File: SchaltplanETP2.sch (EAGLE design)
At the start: 59 parts, among them IC1 LM2674, IC2 ZXLD1350, IC3 ZXLD1350, IC4 ZXLD1350, IC5 ZXLD1350, M1 RN42_BLUETOOTH, T1 BUK98150-55A

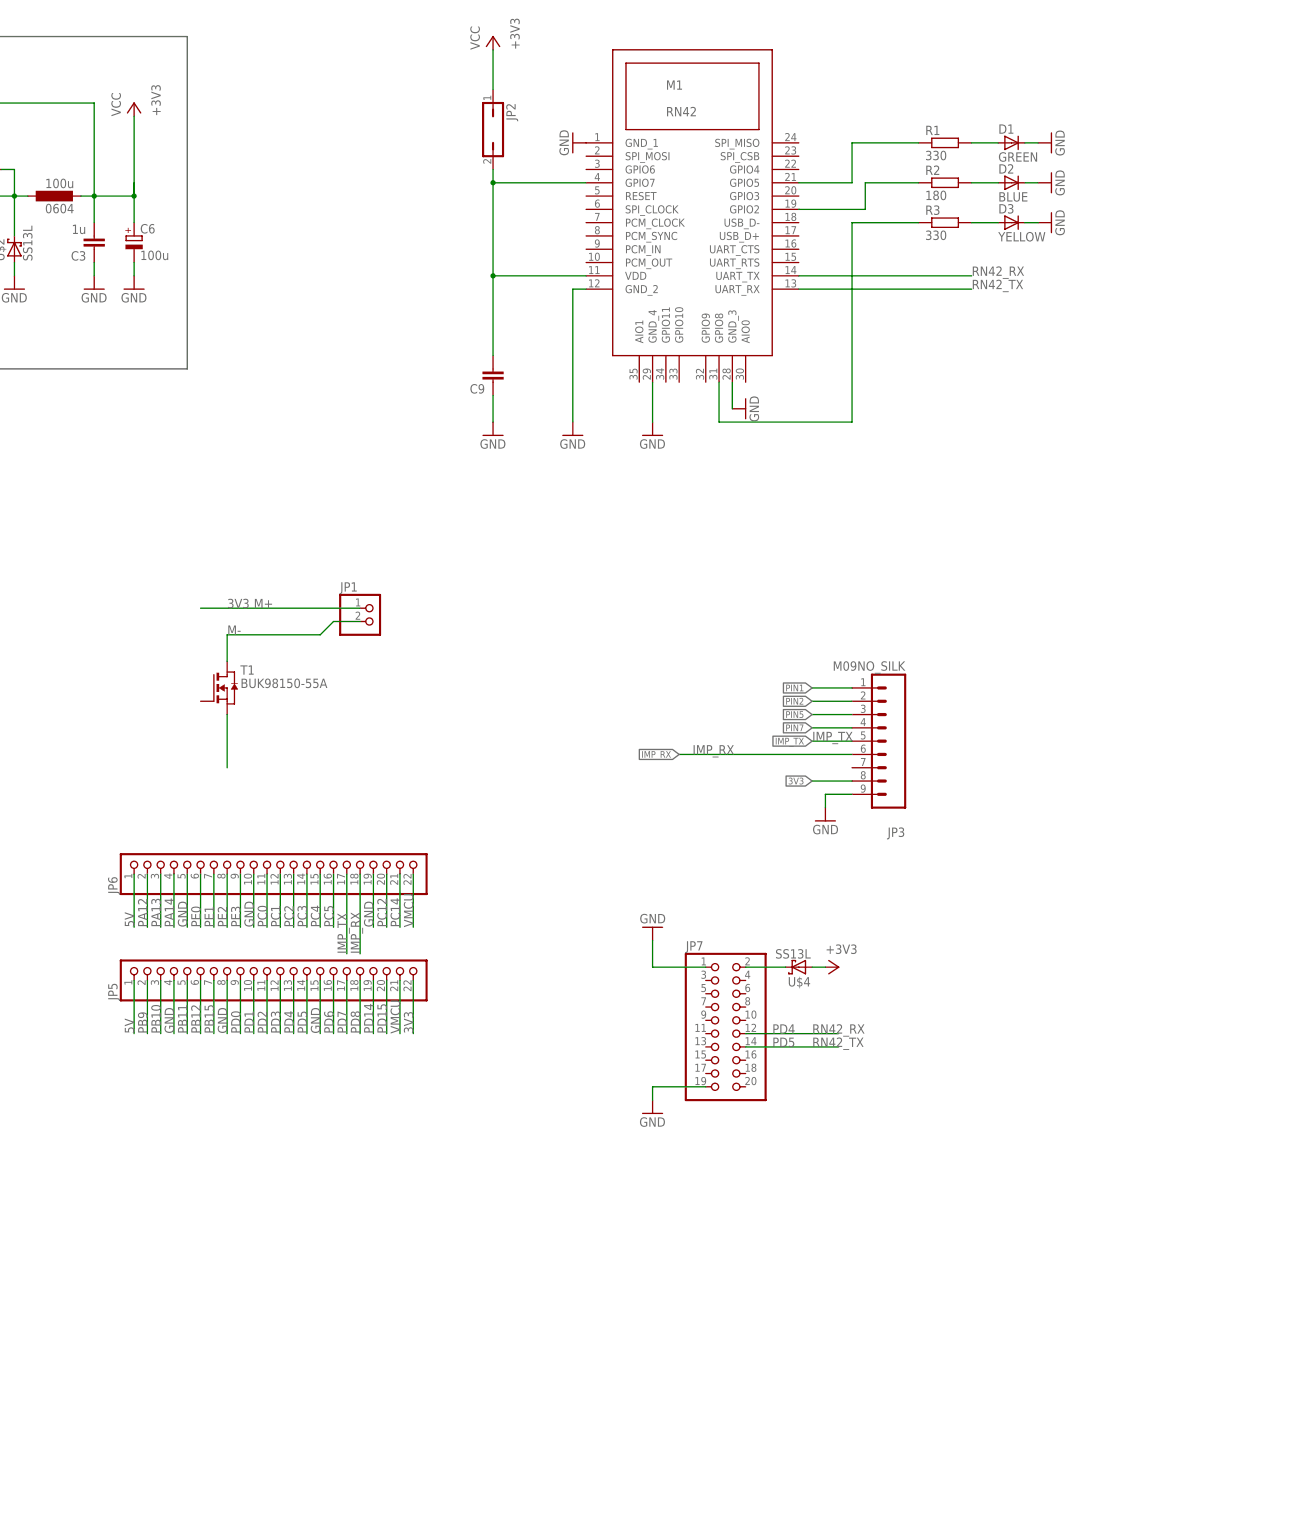
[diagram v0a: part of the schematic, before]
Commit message: Changed LED of pin 21 from the RN42 module to fit the datasheet. Added Jumpber behind DC-Jack to allow direct soldering of cables. Added Terminal Blocks for LEDs.
Placed part onto grid.
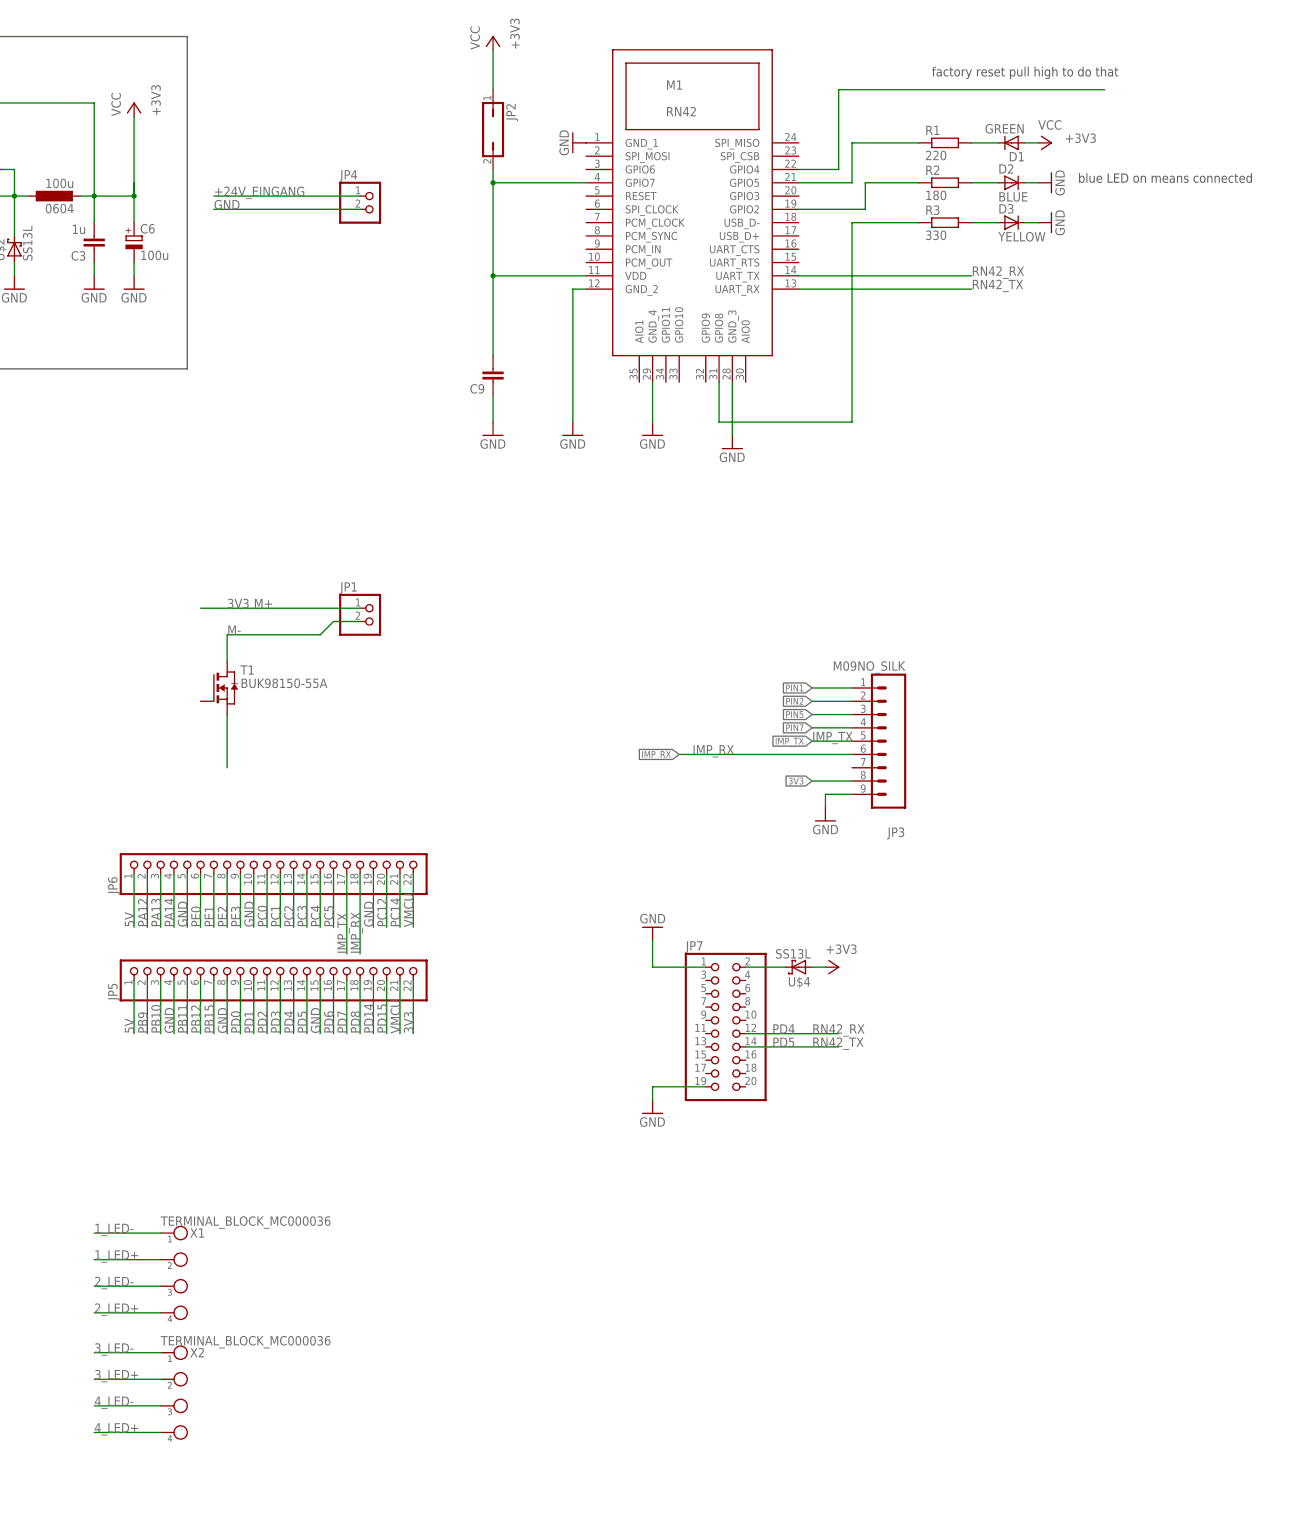
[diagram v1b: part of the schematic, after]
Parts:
- added JP4: (no value), pinhead:PINHD-1X2
- added X1, X2: TERMINAL_BLOCK_MC000036, Moodlight:TERMINAL_BLOCK_MC000036
- R1: value 330 -> 220
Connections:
- removed net N$1: U$1.A, U$3.1
- new net +24V_EINGANG: JP4.1, U$1.A, U$3.1
- new net 4_LED+: X2.4
- new net 4_LED-: X2.3
- new net N$21: M1.GPIO4
- net +3V3: now also D1.A
- net 1_LED+: now also X1.2
- net 1_LED-: now also X1.1
- net 2_LED+: now also X1.4
- net 2_LED-: now also X1.3
- net 3_LED+: now also X2.2
- net 3_LED-: now also X2.1
- net GND: now also JP4.2; no longer D1.C
- net N$7: now also D1.C; no longer D1.A
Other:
- note added: "blue LED on means connected"
- note added: "factory reset pull high to do that"
- moved on the sheet: D1
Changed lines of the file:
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@@
 <layer number="91" name="Nets" color="2" fill="1" visible="yes" active="yes"/>
 <layer number="92" name="Busses" color="1" fill="1" visible="yes" active="yes"/>
-<layer number="93" name="Pins" color="2" fill="1" visible="yes" active="yes"/>
+<layer number="93" name="Pins" color="2" fill="1" visible="no" active="yes"/>
 <layer number="94" name="Symbols" color="4" fill="1" visible="yes" active="yes"/>
 <layer number="95" name="Names" color="7" fill="1" visible="yes" active="yes"/>
@@
 <part name="GND16" library="supply1" deviceset="GND" device=""/>
 <part name="GND17" library="supply1" deviceset="GND" device=""/>
-<part name="GND18" library="supply1" deviceset="GND" device=""/>
 <part name="JP2" library="jumper" deviceset="JP1Q" device=""/>
 <part name="P+2" library="supply1" deviceset="VCC" device=""/>
 <part name="C9" library="rcl" deviceset="C-EU" device="C1808"/>
-<part name="R1" library="rcl" deviceset="R-EU_" device="R0603" value="330"/>
+<part name="R1" library="rcl" deviceset="R-EU_" device="R0603" value="220"/>
 <part name="R2" library="rcl" deviceset="R-EU_" device="R0603" value="180"/>
 <part name="R3" library="rcl" deviceset="R-EU_" device="R0603" value="330"/>
@@
 <part name="JP1" library="pinhead" deviceset="PINHD-1X2" device=""/>
 <part name="T1" library="Moodlight" deviceset="BUK98150-55A" device=""/>
+<part name="P+7" library="supply1" deviceset="VCC" device=""/>
+<part name="X1" library="Moodlight" deviceset="TERMINAL_BLOCK_MC000036" device=""/>
+<part name="X2" library="Moodlight" deviceset="TERMINAL_BLOCK_MC000036" device=""/>
+<part name="JP4" library="pinhead" deviceset="PINHD-1X2" device=""/>
 </parts>
 <sheets>
@@
 <text x="-38.1" y="-241.3" size="1.778" layer="97">F_g 1000Hz</text>
 <text x="88.9" y="30.48" size="1.778" layer="95">M+</text>
+<text x="246.38" y="111.76" size="1.778" layer="97">blue LED on means connected</text>
+<text x="218.44" y="132.08" size="1.778" layer="97">factory reset pull high to do that</text>
 </plain>
 <instances>
@@
 <instance part="GND13" gate="1" x="149.86" y="63.5"/>
 <instance part="GND14" gate="1" x="165.1" y="63.5"/>
-<instance part="GND15" gate="1" x="182.88" y="68.58" rot="R90"/>
+<instance part="GND15" gate="1" x="180.34" y="60.96"/>
 <instance part="GND16" gate="1" x="241.3" y="104.14" rot="R90"/>
 <instance part="GND17" gate="1" x="241.3" y="111.76" rot="R90"/>
-<instance part="GND18" gate="1" x="241.3" y="119.38" rot="R90"/>
 <instance part="JP2" gate="A" x="134.62" y="121.92" rot="R180"/>
 <instance part="P+2" gate="VCC" x="134.62" y="139.7"/>
@@
 <instance part="R2" gate="G$1" x="220.98" y="111.76"/>
 <instance part="R3" gate="G$1" x="220.98" y="104.14"/>
-<instance part="D1" gate="G$1" x="233.68" y="119.38"/>
+<instance part="D1" gate="G$1" x="233.68" y="119.38" rot="R180"/>
 <instance part="D2" gate="G$1" x="233.68" y="111.76"/>
 <instance part="D3" gate="G$1" x="233.68" y="104.14"/>
@@
 <instance part="JP1" gate="G$1" x="111.76" y="27.94"/>
 <instance part="T1" gate="G$1" x="83.82" y="15.24"/>
+<instance part="P+7" gate="VCC" x="241.3" y="119.38" rot="R270"/>
+<instance part="X1" gate="1" x="73.66" y="-88.9"/>
+<instance part="X2" gate="1" x="73.66" y="-111.76"/>
+<instance part="JP4" gate="G$1" x="111.76" y="106.68"/>
 </instances>
 <busses>
@@
 <pinref part="M1" gate="G$1" pin="GND_3"/>
 <pinref part="GND15" gate="1" pin="GND"/>
-<wire x1="180.34" y1="68.58" x2="180.34" y2="73.66" width="0.1524" layer="91"/>
+<wire x1="180.34" y1="63.5" x2="180.34" y2="73.66" width="0.1524" layer="91"/>
 </segment>
 <segment>
@@
 </segment>
 <segment>
-<pinref part="GND18" gate="1" pin="GND"/>
-<pinref part="D1" gate="G$1" pin="C"/>
-<wire x1="236.22" y1="119.38" x2="238.76" y2="119.38" width="0.1524" layer="91"/>
-</segment>
-<segment>
 <pinref part="GND17" gate="1" pin="GND"/>
 <pinref part="D2" gate="G$1" pin="C"/>
@@
 <pinref part="GND31" gate="1" pin="GND"/>
 <wire x1="-33.02" y1="-228.6" x2="-33.02" y2="-226.06" width="0.1524" layer="91"/>
+</segment>
+<segment>
+<pinref part="JP4" gate="G$1" pin="2"/>
+<wire x1="109.22" y1="106.68" x2="81.28" y2="106.68" width="0.1524" layer="91"/>
+<label x="81.28" y="106.68" size="1.778" layer="95"/>
 </segment>
 </net>
@@
 </segment>
 </net>
-<net name="N$1" class="0">
+<net name="+24V_EINGANG" class="0">
 <segment>
 <pinref part="U$3" gate="G$1" pin="1"/>
 <pinref part="U$1" gate="G$1" pin="A"/>
 <wire x1="-38.1" y1="111.76" x2="-43.18" y2="111.76" width="0.1524" layer="91"/>
+</segment>
+<segment>
+<pinref part="JP4" gate="G$1" pin="1"/>
+<wire x1="109.22" y1="109.22" x2="81.28" y2="109.22" width="0.1524" layer="91"/>
+<label x="81.28" y="109.22" size="1.778" layer="95"/>
 </segment>
 </net>
@@
 <label x="139.7" y="137.16" size="1.778" layer="95" rot="R90"/>
 </segment>
+<segment>
+<pinref part="D1" gate="G$1" pin="A"/>
+<pinref part="P+7" gate="VCC" pin="VCC"/>
+<wire x1="238.76" y1="119.38" x2="236.22" y2="119.38" width="0.1524" layer="91"/>
+<label x="243.84" y="119.38" size="1.778" layer="95"/>
+</segment>
 </net>
 <net name="N$3" class="0">
@@
 <junction x="134.62" y="93.98"/>
 <junction x="134.62" y="111.76"/>
-</segment>
-</net>
-<net name="N$7" class="0">
-<segment>
-<pinref part="R1" gate="G$1" pin="2"/>
-<pinref part="D1" gate="G$1" pin="A"/>
-<wire x1="231.14" y1="119.38" x2="226.06" y2="119.38" width="0.1524" layer="91"/>
 </segment>
 </net>
@@
 <label x="-7.62" y="-208.28" size="1.778" layer="95" rot="R90"/>
 </segment>
+<segment>
+<pinref part="X2" gate="1" pin="2"/>
+<wire x1="71.12" y1="-116.84" x2="58.42" y2="-116.84" width="0.1524" layer="91"/>
+<label x="58.42" y="-116.84" size="1.778" layer="95"/>
+</segment>
 </net>
 <net name="3_LED-" class="0">
@@
 <junction x="0" y="-218.44"/>
 </segment>
+<segment>
+<pinref part="X2" gate="1" pin="1"/>
+<wire x1="71.12" y1="-111.76" x2="58.42" y2="-111.76" width="0.1524" layer="91"/>
+<label x="58.42" y="-111.76" size="1.778" layer="95"/>
+</segment>
 </net>
 <net name="2_LED-" class="0">
@@
 <wire x1="0" y1="-134.62" x2="0" y2="-121.92" width="0.1524" layer="91"/>
 <junction x="0" y="-134.62"/>
+</segment>
+<segment>
+<pinref part="X1" gate="1" pin="3"/>
+<wire x1="71.12" y1="-99.06" x2="58.42" y2="-99.06" width="0.1524" layer="91"/>
+<label x="58.42" y="-99.06" size="1.778" layer="95"/>
 </segment>
 </net>
@@
 <label x="-7.62" y="-124.46" size="1.778" layer="95" rot="R90"/>
 </segment>
+<segment>
+<pinref part="X1" gate="1" pin="4"/>
+<wire x1="71.12" y1="-104.14" x2="58.42" y2="-104.14" width="0.1524" layer="91"/>
+<label x="58.42" y="-104.14" size="1.778" layer="95"/>
+</segment>
 </net>
 <net name="1_LED+" class="0">
@@
 <label x="-7.62" y="-40.64" size="1.778" layer="95" rot="R90"/>
 </segment>
+<segment>
+<pinref part="X1" gate="1" pin="2"/>
+<wire x1="71.12" y1="-93.98" x2="58.42" y2="-93.98" width="0.1524" layer="91"/>
+<label x="58.42" y="-93.98" size="1.778" layer="95"/>
+</segment>
 </net>
 <net name="1_LED-" class="0">
@@
 <wire x1="0" y1="-50.8" x2="0" y2="-38.1" width="0.1524" layer="91"/>
 <junction x="0" y="-50.8"/>
+</segment>
+<segment>
+<pinref part="X1" gate="1" pin="1"/>
+<wire x1="71.12" y1="-88.9" x2="58.42" y2="-88.9" width="0.1524" layer="91"/>
+<label x="58.42" y="-88.9" size="1.778" layer="95"/>
 </segment>
 </net>
@@
 </segment>
 </net>
+<net name="N$21" class="0">
+<segment>
+<pinref part="M1" gate="G$1" pin="GPIO4"/>
+<wire x1="193.04" y1="114.3" x2="200.66" y2="114.3" width="0.1524" layer="91"/>
+<wire x1="200.66" y1="114.3" x2="200.66" y2="129.54" width="0.1524" layer="91"/>
+<wire x1="200.66" y1="129.54" x2="251.46" y2="129.54" width="0.1524" layer="91"/>
+</segment>
+</net>
+<net name="N$7" class="0">
+<segment>
+<pinref part="R1" gate="G$1" pin="2"/>
+<pinref part="D1" gate="G$1" pin="C"/>
+<wire x1="231.14" y1="119.38" x2="226.06" y2="119.38" width="0.1524" layer="91"/>
+</segment>
+</net>
+<net name="4_LED-" class="0">
+<segment>
+<pinref part="X2" gate="1" pin="3"/>
+<wire x1="71.12" y1="-121.92" x2="58.42" y2="-121.92" width="0.1524" layer="91"/>
+<label x="58.42" y="-121.92" size="1.778" layer="95"/>
+</segment>
+</net>
+<net name="4_LED+" class="0">
+<segment>
+<pinref part="X2" gate="1" pin="4"/>
+<wire x1="71.12" y1="-127" x2="58.42" y2="-127" width="0.1524" layer="91"/>
+<label x="58.42" y="-127" size="1.778" layer="95"/>
+</segment>
+</net>
